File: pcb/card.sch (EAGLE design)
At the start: 23 parts, among them IC1 74HC14D, IC2 24LC256SN, Q1 BC817

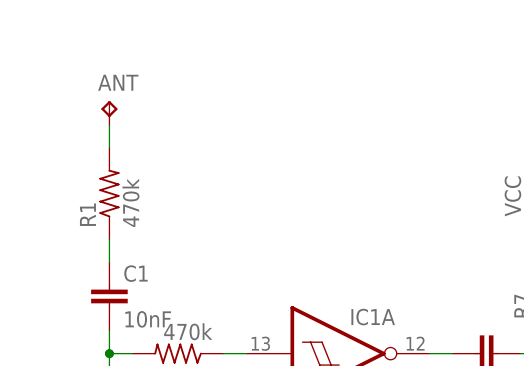
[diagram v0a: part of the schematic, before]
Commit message: Adjusted the PCB size & improved the design.
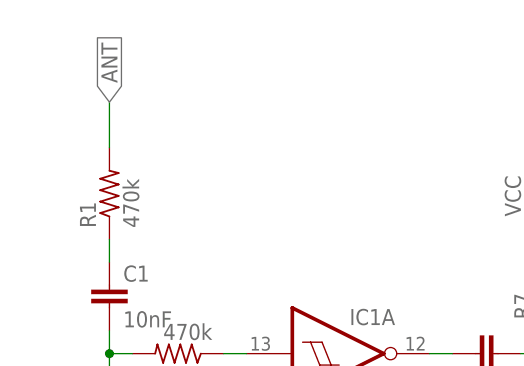
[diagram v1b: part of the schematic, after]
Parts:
- removed ANT: TPB1,27, testpad:TPB1,27
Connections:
- net ANT: no longer ANT.TP
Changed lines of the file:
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@@
 <part name="R4" library="resistor" deviceset="R-US_" device="M1206" value="10M"/>
 <part name="R5" library="resistor" deviceset="R-US_" device="M1206" value="10M"/>
-<part name="ANT" library="testpad" deviceset="TP" device="B1,27"/>
 <part name="BAT" library="bat" deviceset="KB3003" device=""/>
 </parts>
@@
 <instance part="R4" gate="G$1" x="-22.86" y="30.48"/>
 <instance part="R5" gate="G$1" x="-22.86" y="22.86" rot="R180"/>
-<instance part="ANT" gate="G$1" x="-17.78" y="78.74"/>
 <instance part="BAT" gate="G$1" x="45.72" y="10.16"/>
 </instances>
@@
 <segment>
 <pinref part="R1" gate="G$1" pin="2"/>
-<wire x1="-17.78" y1="76.2" x2="-17.78" y2="73.66" width="0.1524" layer="91"/>
-<pinref part="ANT" gate="G$1" pin="TP"/>
+<wire x1="-17.78" y1="73.66" x2="-17.78" y2="78.74" width="0.1524" layer="91"/>
+<label x="-17.78" y="78.74" size="1.778" layer="95" rot="R90" xref="yes"/>
 </segment>
 </net>

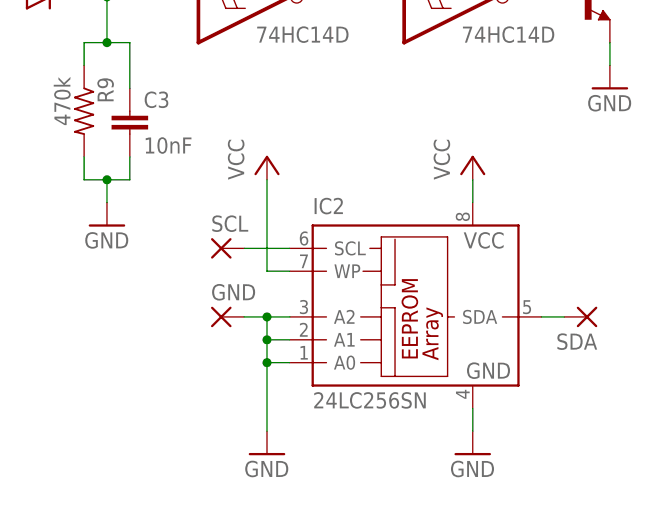
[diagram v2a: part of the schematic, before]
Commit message: Reduced spacing and changed the shape of resume testpads.
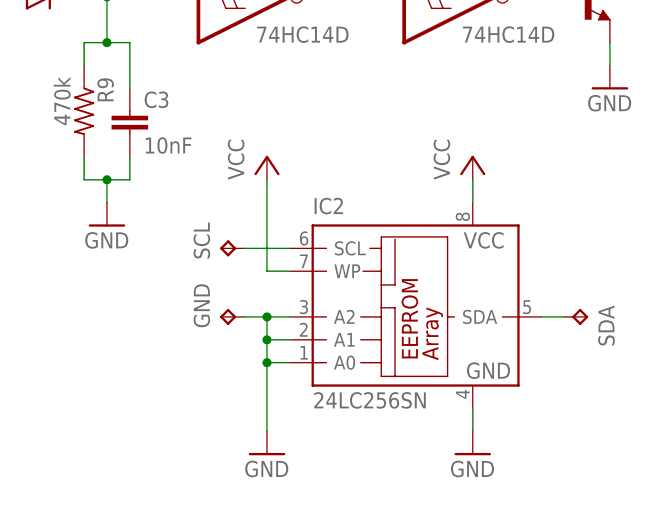
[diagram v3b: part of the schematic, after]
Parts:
- GND, SCL, SDA: value (none) -> TPB1,27; device wirepad:SMD2 -> testpad:TPB1,27
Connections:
- net GND: now also GND.TP; no longer GND.P
- net N$10: now also SDA.TP; no longer SDA.P
- net N$9: now also SCL.TP; no longer SCL.P
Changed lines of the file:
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@@
 <part name="GND7" library="supply1" deviceset="GND" device=""/>
 <part name="P+5" library="supply1" deviceset="VCC" device=""/>
-<part name="SDA" library="wirepad" deviceset="SMD2" device=""/>
-<part name="SCL" library="wirepad" deviceset="SMD2" device=""/>
 <part name="IC2" library="microchip" deviceset="24*" device="SN" technology="LC256"/>
-<part name="GND" library="wirepad" deviceset="SMD2" device=""/>
 <part name="C1" library="resistor" deviceset="C-EU" device="C1206K" value="10nF"/>
 <part name="R3" library="resistor" deviceset="R-US_" device="M1206" value="10M"/>
@@
 <part name="R5" library="resistor" deviceset="R-US_" device="M1206" value="10M"/>
 <part name="BAT" library="bat" deviceset="KB3003" device=""/>
+<part name="SCL" library="testpad" deviceset="TP" device="B1,27"/>
+<part name="GND" library="testpad" deviceset="TP" device="B1,27"/>
+<part name="SDA" library="testpad" deviceset="TP" device="B1,27"/>
 </parts>
 <sheets>
@@
 <instance part="GND7" gate="1" x="99.06" y="0"/>
 <instance part="P+5" gate="VCC" x="99.06" y="33.02"/>
-<instance part="SDA" gate="1" x="134.62" y="15.24" rot="R180"/>
-<instance part="SCL" gate="1" x="93.98" y="22.86"/>
 <instance part="IC2" gate="G$1" x="114.3" y="15.24"/>
-<instance part="GND" gate="1" x="93.98" y="15.24"/>
 <instance part="C1" gate="G$1" x="-17.78" y="58.42"/>
 <instance part="R3" gate="G$1" x="-22.86" y="38.1" rot="R180"/>
@@
 <instance part="R5" gate="G$1" x="-22.86" y="22.86" rot="R180"/>
 <instance part="BAT" gate="G$1" x="45.72" y="10.16"/>
+<instance part="SCL" gate="G$1" x="93.98" y="22.86" rot="R90"/>
+<instance part="GND" gate="G$1" x="93.98" y="15.24" rot="R90"/>
+<instance part="SDA" gate="G$1" x="134.62" y="15.24" rot="R270"/>
 </instances>
 <busses>
@@
 <pinref part="IC2" gate="G$1" pin="A1"/>
 <pinref part="IC2" gate="G$1" pin="A2"/>
-<pinref part="GND" gate="1" pin="P"/>
 <wire x1="99.06" y1="15.24" x2="96.52" y2="15.24" width="0.1524" layer="91"/>
 <junction x="99.06" y="15.24"/>
+<pinref part="GND" gate="G$1" pin="TP"/>
 </segment>
 <segment>
@@
 <segment>
 <wire x1="101.6" y1="22.86" x2="96.52" y2="22.86" width="0.1524" layer="91"/>
-<pinref part="SCL" gate="1" pin="P"/>
 <pinref part="IC2" gate="G$1" pin="SCL"/>
+<pinref part="SCL" gate="G$1" pin="TP"/>
 </segment>
 </net>
@@
 <segment>
 <wire x1="132.08" y1="15.24" x2="129.54" y2="15.24" width="0.1524" layer="91"/>
-<pinref part="SDA" gate="1" pin="P"/>
 <pinref part="IC2" gate="G$1" pin="SDA"/>
-</segment>
-</net>
+<pinref part="SDA" gate="G$1" pin="TP"/>
+</segment>
+</net>

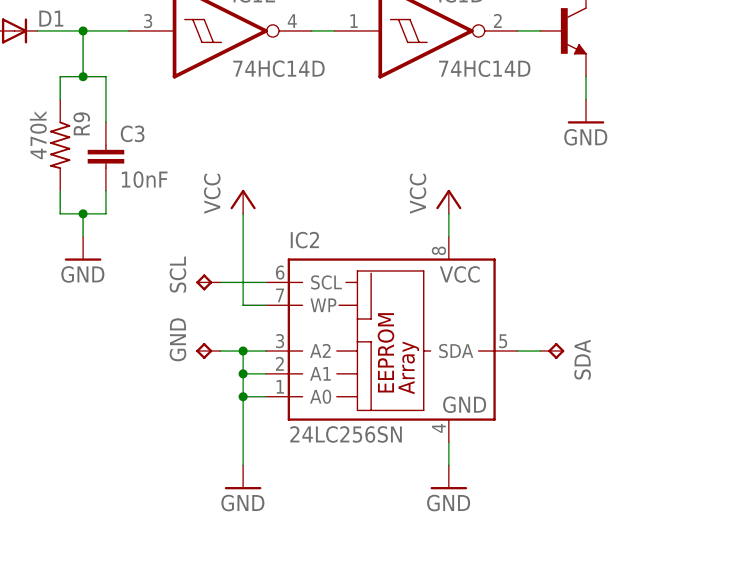
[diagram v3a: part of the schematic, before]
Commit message: Swapped I2C EEPROM for SPI Flash & adjusted the design accordingly.
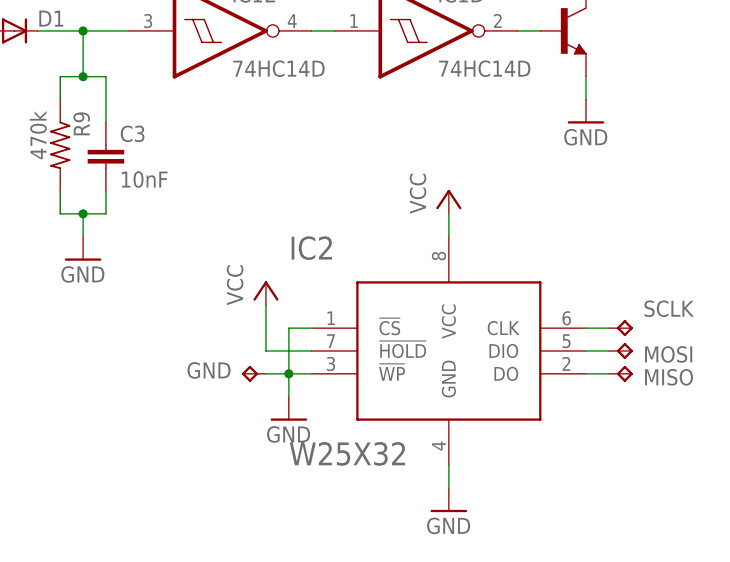
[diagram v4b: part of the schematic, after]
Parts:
- removed SCL, SDA: TPB1,27, testpad:TPB1,27
- added MISO, MOSI, SCLK: TPB1,27, testpad:TPB1,27
- IC2: value 24LC256SN -> W25X32; device microchip:24LC256SN -> bat:W25X32
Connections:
- new net N$88: IC2.DO, MISO.TP
- net GND: now also IC2.!CS!, IC2.!WP!; no longer IC2.A0, IC2.A1, IC2.A2
- net N$10: now also IC2.CLK, SCLK.TP; no longer IC2.SDA, SDA.TP
- net N$9: now also IC2.DIO, MOSI.TP; no longer IC2.SCL, SCL.TP
- net VCC: now also IC2.!HOLD!; no longer IC2.WP
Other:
- moved on the sheet: GND
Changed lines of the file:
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@@
 <part name="GND7" library="supply1" deviceset="GND" device=""/>
 <part name="P+5" library="supply1" deviceset="VCC" device=""/>
-<part name="IC2" library="microchip" deviceset="24*" device="SN" technology="LC256"/>
 <part name="C1" library="resistor" deviceset="C-EU" device="C1206K" value="10nF"/>
 <part name="R3" library="resistor" deviceset="R-US_" device="M1206" value="10M"/>
@@
 <part name="R5" library="resistor" deviceset="R-US_" device="M1206" value="10M"/>
 <part name="BAT" library="bat" deviceset="KB3003" device=""/>
-<part name="SCL" library="testpad" deviceset="TP" device="B1,27"/>
+<part name="MISO" library="testpad" deviceset="TP" device="B1,27"/>
+<part name="MOSI" library="testpad" deviceset="TP" device="B1,27"/>
+<part name="SCLK" library="testpad" deviceset="TP" device="B1,27"/>
+<part name="IC2" library="bat" deviceset="W25X32" device=""/>
 <part name="GND" library="testpad" deviceset="TP" device="B1,27"/>
-<part name="SDA" library="testpad" deviceset="TP" device="B1,27"/>
 </parts>
 <sheets>
@@
 <instance part="C3" gate="G$1" x="83.82" y="38.1"/>
 <instance part="P+4" gate="VCC" x="121.92" y="33.02"/>
-<instance part="GND6" gate="1" x="121.92" y="0"/>
-<instance part="GND7" gate="1" x="99.06" y="0"/>
-<instance part="P+5" gate="VCC" x="99.06" y="33.02"/>
-<instance part="IC2" gate="G$1" x="114.3" y="15.24"/>
+<instance part="GND6" gate="1" x="121.92" y="-2.54"/>
+<instance part="GND7" gate="1" x="104.14" y="7.62"/>
+<instance part="P+5" gate="VCC" x="101.6" y="22.86"/>
 <instance part="C1" gate="G$1" x="-17.78" y="58.42"/>
 <instance part="R3" gate="G$1" x="-22.86" y="38.1" rot="R180"/>
@@
 <instance part="R5" gate="G$1" x="-22.86" y="22.86" rot="R180"/>
 <instance part="BAT" gate="G$1" x="45.72" y="10.16"/>
-<instance part="SCL" gate="G$1" x="93.98" y="22.86" rot="R90"/>
-<instance part="GND" gate="G$1" x="93.98" y="15.24" rot="R90"/>
-<instance part="SDA" gate="G$1" x="134.62" y="15.24" rot="R270"/>
+<instance part="MISO" gate="G$1" x="142.24" y="12.7" smashed="yes" rot="R270">
+<attribute name="NAME" x="143.51" y="11.43" size="1.778" layer="95"/>
+<attribute name="TP_SIGNAL_NAME" x="140.97" y="11.43" size="1.778" layer="97" rot="R270"/>
+</instance>
+<instance part="MOSI" gate="G$1" x="142.24" y="15.24" smashed="yes" rot="R270">
+<attribute name="NAME" x="143.51" y="13.97" size="1.778" layer="95"/>
+<attribute name="TP_SIGNAL_NAME" x="140.97" y="13.97" size="1.778" layer="97" rot="R270"/>
+</instance>
+<instance part="SCLK" gate="G$1" x="142.24" y="17.78" smashed="yes" rot="R270">
+<attribute name="NAME" x="143.51" y="19.05" size="1.778" layer="95"/>
+<attribute name="TP_SIGNAL_NAME" x="140.97" y="16.51" size="1.778" layer="97" rot="R270"/>
+</instance>
+<instance part="IC2" gate="G$1" x="121.92" y="15.24"/>
+<instance part="GND" gate="G$1" x="99.06" y="12.7" smashed="yes" rot="R90">
+<attribute name="NAME" x="97.79" y="13.97" size="1.778" layer="95" rot="R180"/>
+<attribute name="TP_SIGNAL_NAME" x="100.33" y="13.97" size="1.778" layer="97" rot="R90"/>
+</instance>
 </instances>
 <busses>
@@
 </segment>
 <segment>
-<pinref part="GND7" gate="1" pin="GND"/>
-<wire x1="101.6" y1="15.24" x2="99.06" y2="15.24" width="0.1524" layer="91"/>
-<wire x1="99.06" y1="15.24" x2="99.06" y2="12.7" width="0.1524" layer="91"/>
-<wire x1="99.06" y1="12.7" x2="99.06" y2="10.16" width="0.1524" layer="91"/>
-<wire x1="99.06" y1="10.16" x2="99.06" y2="2.54" width="0.1524" layer="91"/>
-<wire x1="101.6" y1="12.7" x2="99.06" y2="12.7" width="0.1524" layer="91"/>
-<wire x1="101.6" y1="10.16" x2="99.06" y2="10.16" width="0.1524" layer="91"/>
-<junction x="99.06" y="12.7"/>
-<junction x="99.06" y="10.16"/>
-<pinref part="IC2" gate="G$1" pin="A0"/>
-<pinref part="IC2" gate="G$1" pin="A1"/>
-<pinref part="IC2" gate="G$1" pin="A2"/>
-<wire x1="99.06" y1="15.24" x2="96.52" y2="15.24" width="0.1524" layer="91"/>
-<junction x="99.06" y="15.24"/>
-<pinref part="GND" gate="G$1" pin="TP"/>
-</segment>
-<segment>
+<pinref part="GND6" gate="1" pin="GND"/>
 <pinref part="IC2" gate="G$1" pin="GND"/>
-<pinref part="GND6" gate="1" pin="GND"/>
-<wire x1="121.92" y1="5.08" x2="121.92" y2="2.54" width="0.1524" layer="91"/>
+<wire x1="121.92" y1="2.54" x2="121.92" y2="0" width="0.1524" layer="91"/>
 </segment>
 <segment>
@@
 <pinref part="GND2" gate="1" pin="GND"/>
 <wire x1="-17.78" y1="22.86" x2="-17.78" y2="17.78" width="0.1524" layer="91"/>
+</segment>
+<segment>
+<pinref part="IC2" gate="G$1" pin="!WP!"/>
+<wire x1="106.68" y1="12.7" x2="104.14" y2="12.7" width="0.1524" layer="91"/>
+<pinref part="IC2" gate="G$1" pin="!CS!"/>
+<wire x1="104.14" y1="12.7" x2="101.6" y2="12.7" width="0.1524" layer="91"/>
+<wire x1="106.68" y1="17.78" x2="104.14" y2="17.78" width="0.1524" layer="91"/>
+<wire x1="104.14" y1="17.78" x2="104.14" y2="12.7" width="0.1524" layer="91"/>
+<junction x="104.14" y="12.7"/>
+<pinref part="GND" gate="G$1" pin="TP"/>
+<pinref part="GND7" gate="1" pin="GND"/>
+<wire x1="104.14" y1="12.7" x2="104.14" y2="10.16" width="0.1524" layer="91"/>
 </segment>
 </net>
@@
 <segment>
 <pinref part="P+5" gate="VCC" pin="VCC"/>
-<wire x1="101.6" y1="20.32" x2="99.06" y2="20.32" width="0.1524" layer="91"/>
-<wire x1="99.06" y1="20.32" x2="99.06" y2="30.48" width="0.1524" layer="91"/>
-<pinref part="IC2" gate="G$1" pin="WP"/>
+<wire x1="101.6" y1="20.32" x2="101.6" y2="15.24" width="0.1524" layer="91"/>
+<pinref part="IC2" gate="G$1" pin="!HOLD!"/>
+<wire x1="101.6" y1="15.24" x2="106.68" y2="15.24" width="0.1524" layer="91"/>
 </segment>
 </net>
@@
 </segment>
 </net>
-<net name="N$9" class="0">
-<segment>
-<wire x1="101.6" y1="22.86" x2="96.52" y2="22.86" width="0.1524" layer="91"/>
-<pinref part="IC2" gate="G$1" pin="SCL"/>
-<pinref part="SCL" gate="G$1" pin="TP"/>
-</segment>
-</net>
-<net name="N$10" class="0">
-<segment>
-<wire x1="132.08" y1="15.24" x2="129.54" y2="15.24" width="0.1524" layer="91"/>
-<pinref part="IC2" gate="G$1" pin="SDA"/>
-<pinref part="SDA" gate="G$1" pin="TP"/>
-</segment>
-</net>
 <net name="N$1" class="0">
 <segment>
@@
 </segment>
 </net>
+<net name="N$10" class="0">
+<segment>
+<pinref part="IC2" gate="G$1" pin="CLK"/>
+<pinref part="SCLK" gate="G$1" pin="TP"/>
+<wire x1="139.7" y1="17.78" x2="137.16" y2="17.78" width="0.1524" layer="91"/>
+</segment>
+</net>
+<net name="N$9" class="0">
+<segment>
+<pinref part="IC2" gate="G$1" pin="DIO"/>
+<pinref part="MOSI" gate="G$1" pin="TP"/>
+<wire x1="139.7" y1="15.24" x2="137.16" y2="15.24" width="0.1524" layer="91"/>
+</segment>
+</net>
+<net name="N$88" class="0">
+<segment>
+<pinref part="IC2" gate="G$1" pin="DO"/>
+<pinref part="MISO" gate="G$1" pin="TP"/>
+<wire x1="139.7" y1="12.7" x2="137.16" y2="12.7" width="0.1524" layer="91"/>
+</segment>
+</net>

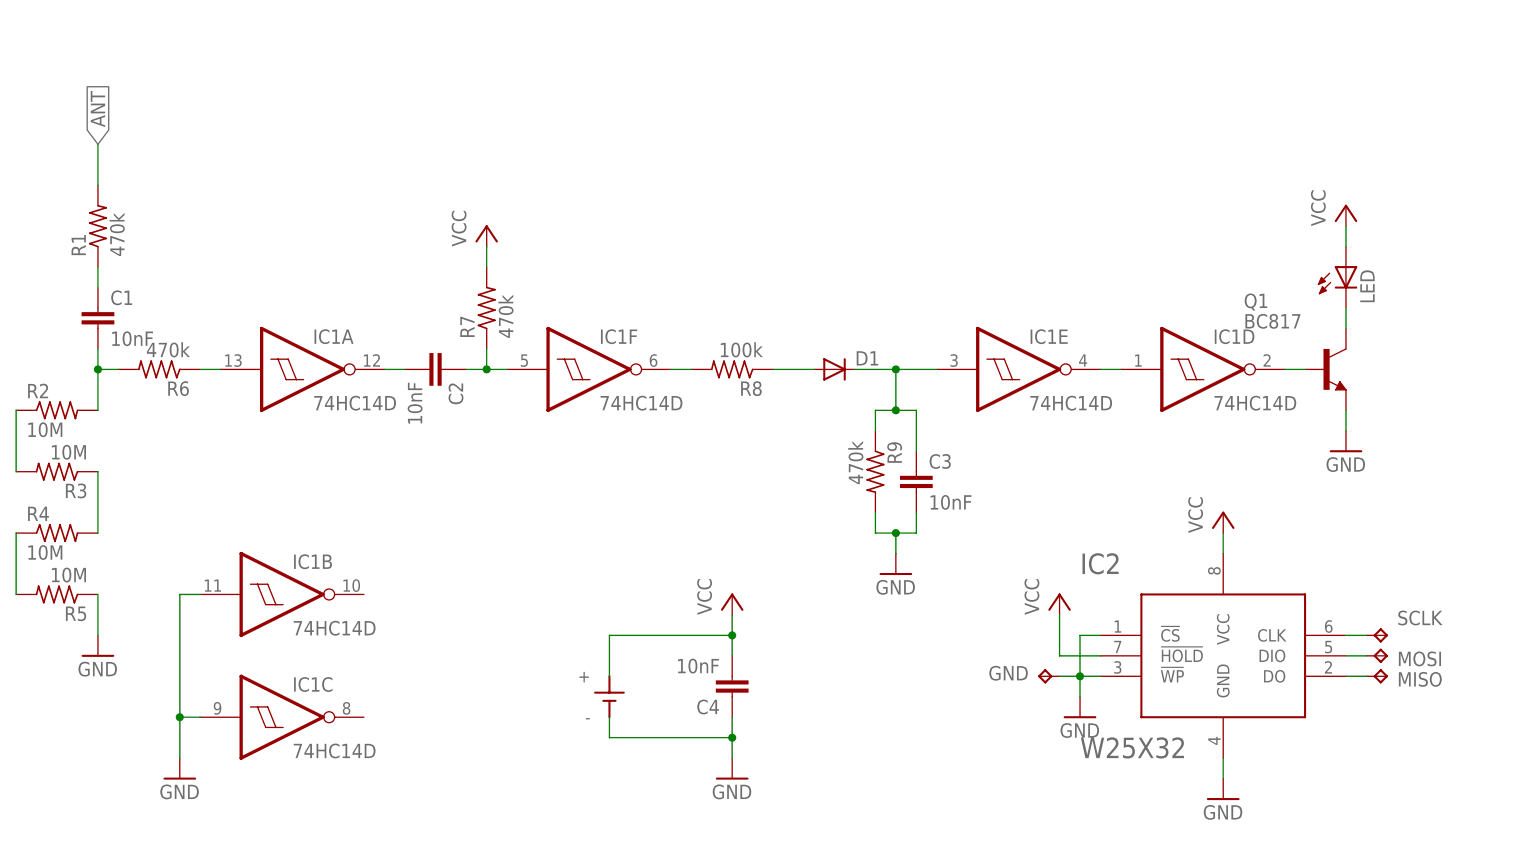
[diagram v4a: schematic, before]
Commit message: Optimized the design.
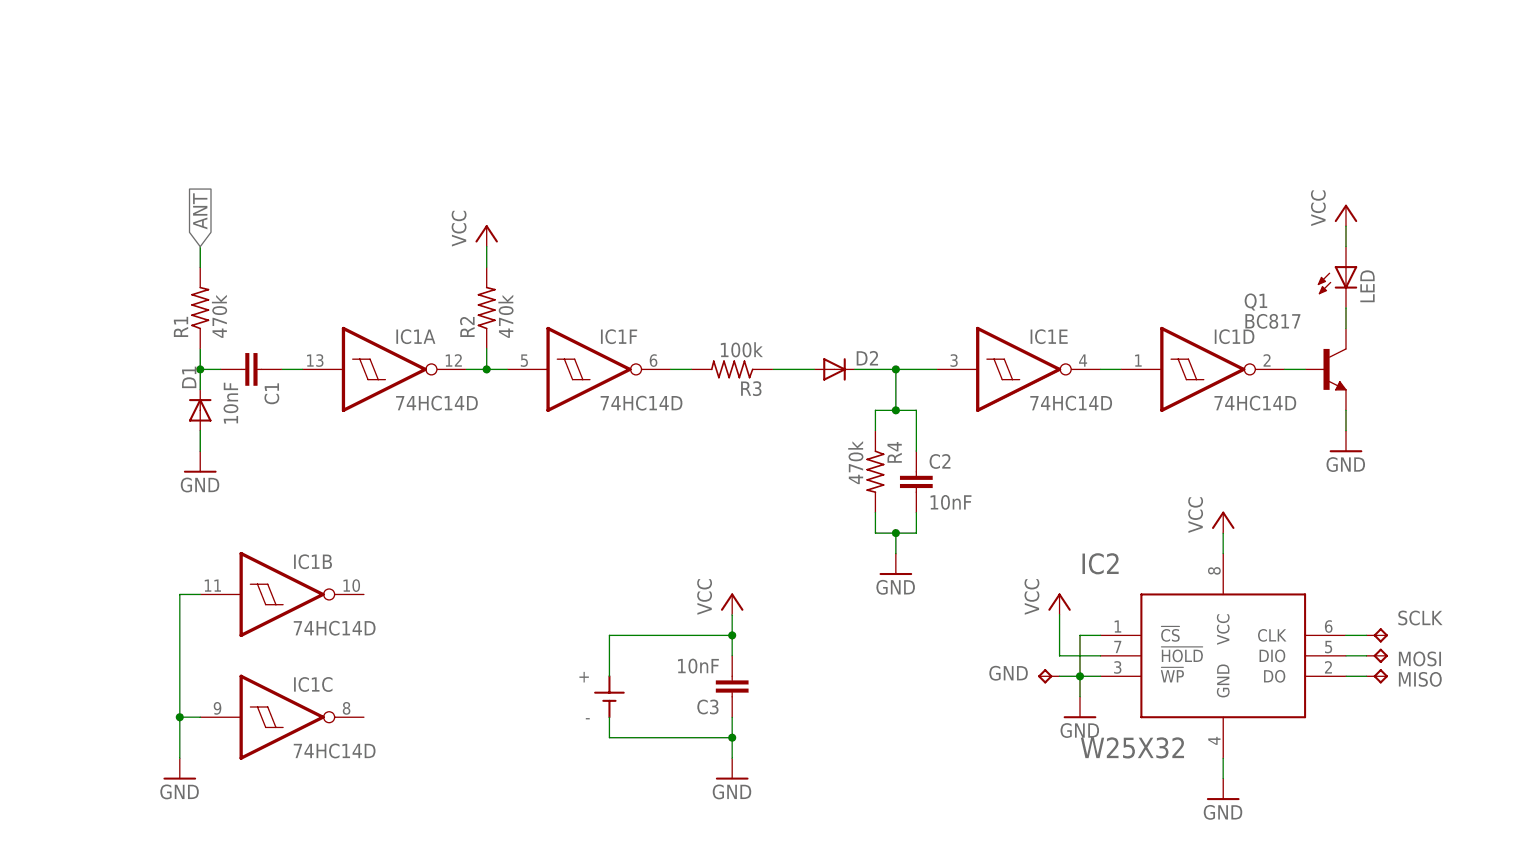
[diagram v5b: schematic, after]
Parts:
- removed C4: 10nF, resistor:C-EUC1206K
- removed R5: 10M, resistor:R-US_M1206
- removed R6, R7, R9: 470k, resistor:R-US_M1206
- removed R8: 100k, resistor:R-US_M1206
- added D2: (no value), diode:DIODE-MINIMELF
- R2, R4: value 10M -> 470k
- R3: value 10M -> 100k
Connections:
- removed net N$14: R2.1, R3.2
- removed net N$15: R3.1, R4.2
- removed net N$16: R4.1, R5.2
- removed net N$3: IC1A.I, R6.1
- removed net N$4: C2.2, IC1A.O
- net GND: now also C2.2, C3.1, D1.A, R4.2; no longer C3.2, C4.1, R5.1, R9.2
- net N$1: now also IC1A.I; no longer R1.1
- net N$2: now also D1.C, R1.1; no longer R2.2, R6.2
- net N$5: now also IC1A.O, R2.1; no longer C2.1, R7.1
- net N$6: now also R3.2; no longer R8.2
- net N$7: now also D2.A, R3.1; no longer D1.A, R8.1
- net N$8: now also C2.1, D2.C, R4.1; no longer C3.1, D1.C, R9.1
- net VCC: now also C3.2, R2.2; no longer C4.2, R7.2
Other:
- moved on the sheet: C1, C2, C3, D1, IC1A, R1, R2, R3, R4
